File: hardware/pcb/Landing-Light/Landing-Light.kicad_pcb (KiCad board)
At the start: 2 copper layers, 70 x 20 mm, 56 parts, among them J1 Conn_01x04, J2 2012670005, Q2 NMOS, Q3 NMOS, Q4 PMOS, SW2 SW_SP3T, SW3 SW_SPDT, U1 BQ25172DSGR, U3 TPS61200DRC

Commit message: v1 Production
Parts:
- moved Q4 0.09 mm to (154.6, 94.2), turned to 90 degrees
- turned JP5 to -90 degrees
- turned R20 to 90 degrees
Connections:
- Q3 pad 1: GND -> -BATT
- Q3 pad 3: -BATT -> GND
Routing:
- net GND: track 43.9 -> 51.7 mm, vias 33 -> 34
- net +5V: track 53.2 -> 51.0 mm
- net Net-(JP6-A): track 7.22 -> 5.26 mm
- net -BATT: track 12.1 -> 11.4 mm
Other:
- board text added: "Landing Light v1.0"
- board text added: "STAT"
- board text added: "TT"

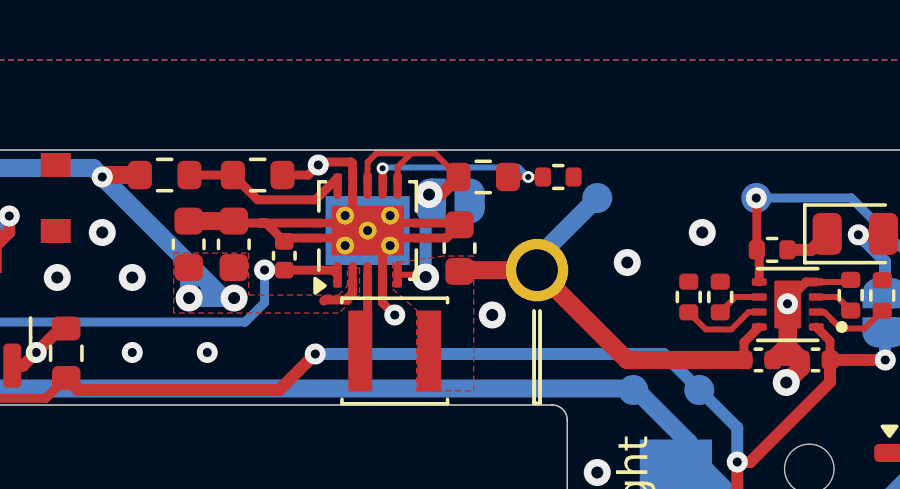
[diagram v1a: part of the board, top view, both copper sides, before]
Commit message: Fix via sizes
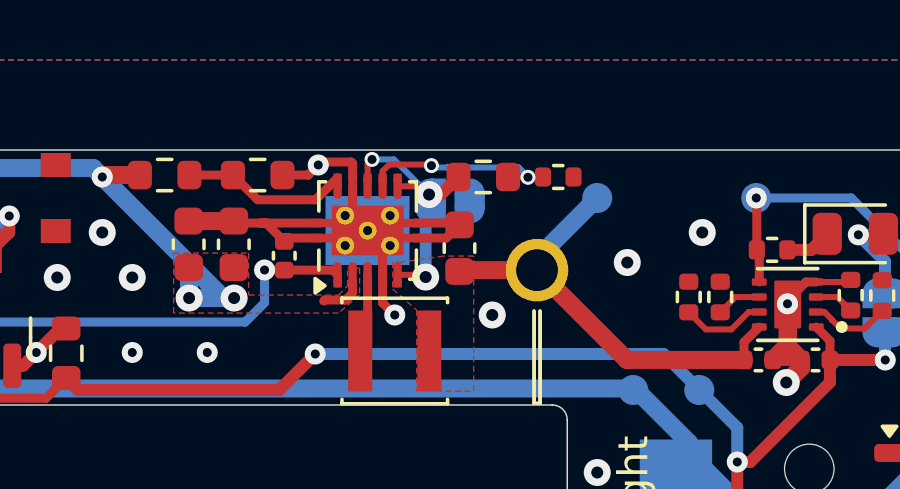
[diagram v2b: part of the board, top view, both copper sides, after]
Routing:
- net +BATT: track 25.3 -> 24.5 mm, vias 2 -> 3
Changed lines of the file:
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@@
-	)
-	(segment
-		(start 168.345 88.566726)
-		(end 168.8 88.111726)
-		(width 0.2)
-		(layer "F.Cu")
-		(net 1)
 	)
 	(segment
@@
 	)
 	(segment
-		(start 169.586726 88.111726)
-		(end 170.375 88.9)
-		(width 0.2)
-		(layer "F.Cu")
-		(net 1)
-	)
-	(segment
-		(start 167.637893 88.111726)
-		(end 168.8 88.111726)
-		(width 0.2)
-		(layer "F.Cu")
-		(net 1)
-	)
-	(segment
 		(start 169.789853 89.485147)
 		(end 170.375 88.9)
@@
 	)
 	(segment
+		(start 169.11794 89.21)
+		(end 169.393087 89.485147)
+		(width 0.2)
+		(layer "F.Cu")
+		(net 1)
+	)
+	(segment
 		(start 179.868 95.022)
 		(end 179.892 94.998)
@@
 	)
 	(segment
-		(start 167.345 88.404619)
-		(end 167.637893 88.111726)
-		(width 0.2)
-		(layer "F.Cu")
-		(net 1)
-	)
-	(segment
 		(start 172.9925 92.005)
 		(end 175.9855 94.998)
@@
 	)
 	(segment
-		(start 168.8 88.111726)
-		(end 169.586726 88.111726)
+		(start 168.345 89.21)
+		(end 169.11794 89.21)
 		(width 0.2)
 		(layer "F.Cu")
@@
 	)
 	(segment
-		(start 168.345 88.925)
-		(end 168.345 88.566726)
+		(start 167.345 88.462537)
+		(end 167.492655 88.314882)
 		(width 0.2)
 		(layer "F.Cu")
@@
 	)
 	(segment
-		(start 167.345 88.925)
-		(end 167.345 88.404619)
-		(width 0.2)
-		(layer "F.Cu")
-		(net 1)
-	)
-	(segment
 		(start 169.205 92.16)
 		(end 169.28 92.235)
@@
 	)
 	(segment
+		(start 167.345 88.925)
+		(end 167.345 88.462537)
+		(width 0.2)
+		(layer "F.Cu")
+		(net 1)
+	)
+	(segment
 		(start 168.345 92.16)
 		(end 169.205 92.16)
@@
 		(net 1)
 	)
+	(via
+		(at 167.492655 88.314882)
+		(size 0.5)
+		(drill 0.3)
+		(layers "F.Cu" "B.Cu")
+		(net 1)
+	)
 	(segment
 		(start 169.28 89.598234)
@@
 	)
 	(segment
+		(start 167.492655 88.314882)
+		(end 168.222822 88.314882)
+		(width 0.2)
+		(layer "B.Cu")
+		(net 1)
+	)
+	(segment
+		(start 168.222822 88.314882)
+		(end 169.393087 89.485147)
+		(width 0.2)
+		(layer "B.Cu")
+		(net 1)
+	)
+	(segment
 		(start 172.9925 91.6075)
 		(end 175 89.6)
@@
 	)
 	(segment
+		(start 169.436927 88.485)
+		(end 168.065 88.485)
+		(width 0.2)
+		(layer "F.Cu")
+		(net 47)
+	)
+	(segment
+		(start 169.471927 88.52)
+		(end 169.436927 88.485)
+		(width 0.2)
+		(layer "F.Cu")
+		(net 47)
+	)
+	(segment
+		(start 168.065 88.485)
+		(end 167.845 88.705)
+		(width 0.2)
+		(layer "F.Cu")
+		(net 47)
+	)
+	(segment
 		(start 172.7 88.9)
+		(end 172.69 88.91)
+		(width 0.2)
+		(layer "F.Cu")
+		(net 47)
+	)
+	(segment
+		(start 172.69 88.91)
 		(end 172.025 88.9)
+		(width 0.2)
+		(layer "F.Cu")
+		(net 47)
+	)
+	(segment
+		(start 167.845 88.705)
+		(end 167.845 88.925)
 		(width 0.2)
 		(layer "F.Cu")
@@
 		(net 47)
 	)
-	(segment
-		(start 167.845 88.611726)
-		(end 167.845 89.21)
-		(width 0.2)
-		(layer "F.Cu")
+	(via
+		(at 169.471927 88.52)
+		(size 0.5)
+		(drill 0.3)
+		(layers "F.Cu" "B.Cu")
 		(net 47)
 	)
 	(via
-		(at 172.7 88.9)
-		(size 0.4)
-		(drill 0.2)
-		(layers "F.Cu" "B.Cu")
-		(net 47)
-	)
-	(via
-		(at 167.845 88.611726)
-		(size 0.4)
-		(drill 0.2)
+		(at 172.69 88.91)
+		(size 0.5)
+		(drill 0.3)
 		(layers "F.Cu" "B.Cu")
 		(net 47)
@@
 	)
 	(segment
-		(start 167.845 88.611726)
-		(end 167.874295 88.582431)
+		(start 169.471927 88.52)
+		(end 169.534358 88.582431)
 		(width 0.2)
 		(layer "B.Cu")
@@
 	)
 	(segment
-		(start 167.874295 88.582431)
+		(start 169.534358 88.582431)
 		(end 170 88.582431)
 		(width 0.2)

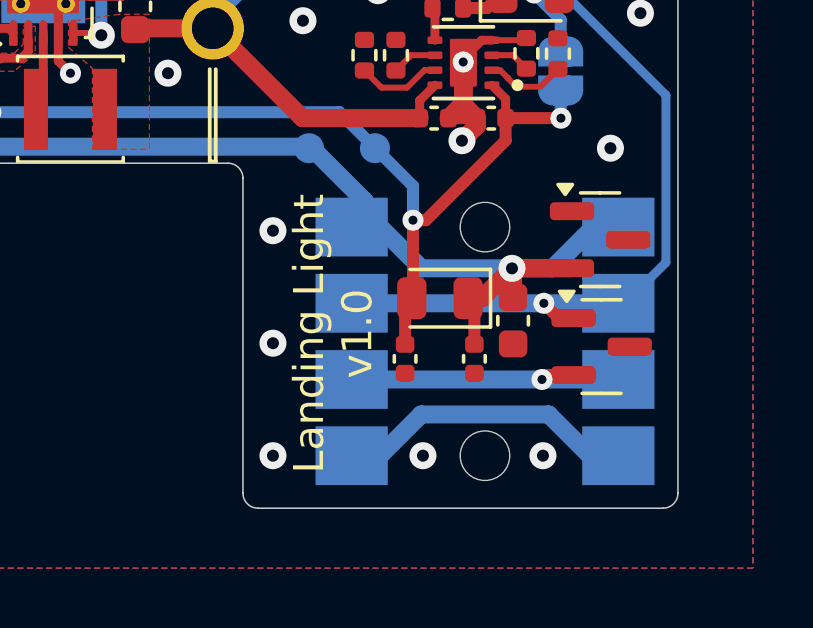
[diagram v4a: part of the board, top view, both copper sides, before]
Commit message: Update power routing
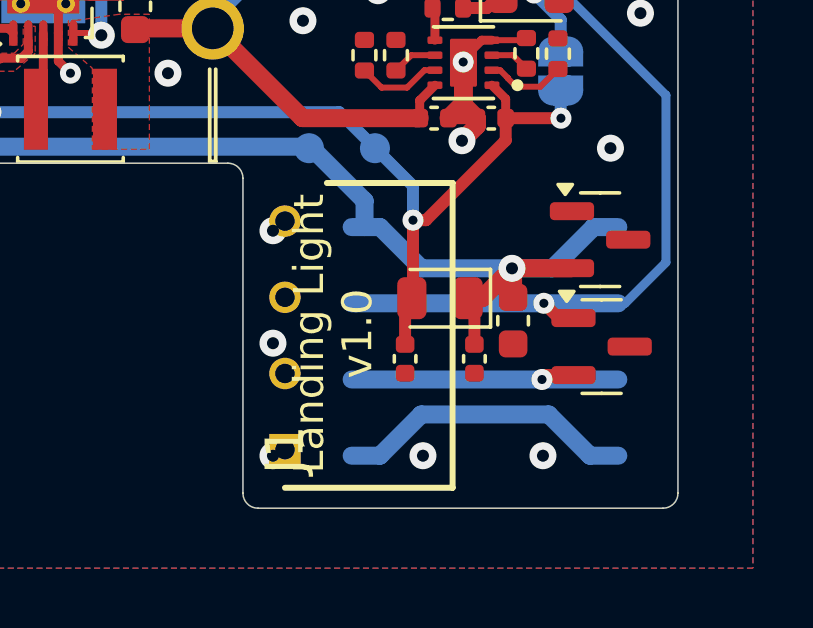
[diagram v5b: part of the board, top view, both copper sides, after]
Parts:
- J1: footprint Landing-Light:70AAJ-4-F1G -> MHCI:399-10-104-10-008000; moved to F.Cu
- moved J1 7.58 mm to (175.4, 106.0), turned to -90 degrees
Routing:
- net DATA2: track 10.0 -> 20.0 mm
- net GND: track 51.7 -> 41.7 mm

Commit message: Complete redesign - starting point
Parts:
- removed D2, D3, D4: D_TVS_Dual_AAC, Package_TO_SOT_SMD:SOT-23
- removed J2: 2012670005, Landing-Light:MOLEX_2012670005
- removed JP3, JP5, JP6: Jumper_2_Open, Jumper:SolderJumper-2_P1.3mm_Open_RoundedPad1.0x1.5mm
- removed R1, R9: 75R, Resistor_SMD:R_0402_1005Metric
- removed SW3: SW_SPDT, Landing-Light:SSSS810201
- added J3: USB_C_Receptacle_USB2.0_16P, Connector_USB:USB_C_Receptacle_G-Switch_GT-USB-7010ASV, F.Cu at (120.8, 101.6)
- added SW1: SW_SPDT, Landing-Light:SSSS810201, F.Cu at (149.0, 89.6)
- added U2: SRV05-4, Package_TO_SOT_SMD:SOT-363_SC-70-6, F.Cu at (177.1, 105.8)
- R8: value 75R -> TC33X-2-501E; footprint Resistor_SMD:R_0402_1005Metric -> Potentiometer_SMD:Potentiometer_Bourns_TC33X_Vertical
- moved TP7 27.3 mm to (203.5, 94.4)
- moved TP2 27.3 mm to (205.7, 94.4)
- moved TP1 25.5 mm to (181.4, 64.9)
- moved L2 24.8 mm to (159.2, 71.6), turned to 0 degrees
- moved R4 22.6 mm to (155.4, 75.7), turned to 90 degrees
- moved TP6 21.4 mm to (168.0, 73.8), turned to 180 degrees
- moved C12 21.1 mm to (157.0, 75.0), turned to -90 degrees
- moved R2 19.1 mm to (191.8, 75.6)
- moved R6 19.1 mm to (192.8, 75.6)
- moved D6 19.1 mm to (191.9, 73.6)
- moved R16 19.1 mm to (189.1, 74.1)
- moved R7 19.1 mm to (187.4, 75.7)
- moved U1 19.1 mm to (189.6, 75.9)
- moved C1 19.1 mm to (190.5, 77.8)
- moved C2 19.1 mm to (188.6, 77.8)
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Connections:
- net Net-(D7-RA) renamed /R
- net Net-(JP4-B) renamed /UVLO
- net Net-(U1-ISET) renamed /ISET
- net Net-(U1-TMR) renamed /TMR
- net Net-(U1-TS) renamed /TS
- net Net-(U1-VSET) renamed /VSET
- net Net-(U3-FB) renamed /FB
- net Net-(U3-L) renamed /L
- C12 pad 1: +BATT -> /VCC_SW
- D7 pad 2: Net-(D7-K) -> /Anode
- D7 pad 3: Net-(D7-GA) -> /G
- D7 pad 4: Net-(D7-BA) -> /B
- JP4 pad 1: +BATT -> /VCC_SW
- L2 pad 1: +BATT -> /VCC_SW
- Q2 pad 1: Net-(JP3-A) -> /Anode_R
- Q4 pad 3: Net-(JP6-A) -> /Anode_R
- R12 pad 1: GND -> /CC1
- R12 pad 2: /CC1 -> GND
- R13 pad 1: Net-(R1-Pad2) -> /R_R
- R3 pad 1: +BATT -> /VCC_SW
- R8 pad 1: Net-(R8-Pad1) -> /Anode
- R8 pad 2: Net-(D7-GA) -> /Anode_R
- SW2 pad 1: Net-(R9-Pad1) -> /B
- SW2 pad 2: Net-(R8-Pad1) -> /G
- SW2 pad 4: Net-(R1-Pad1) -> /R_R
- U3 pad 5: +BATT -> /VCC_SW
- U3 pad 6: +BATT -> /VCC_SW
- U3 pad 8: +BATT -> /VCC_SW
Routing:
- net VIN: track 81.4 -> 0.00 mm, vias 2 -> 0
- net +5V: track 51.0 -> 3.34 mm, vias 3 -> 1
- net VAUX: track 39.9 -> 1.84 mm, vias 2 -> 0
- net +3V3: track 34.5 -> 0.00 mm, vias 4 -> 0
- net Net-(D7-K): track 31.8 -> 0.00 mm, vias 2 -> 0
- net CHARGE_STATUS: track 30.4 -> 1.11 mm, vias 2 -> 0
- net /CC1: track 28.5 -> 0.00 mm, vias 2 -> 0
- net /CC2: track 27.4 -> 0.00 mm, vias 2 -> 0
- net +BATT: track 24.5 -> 1.31 mm, vias 3 -> 0
- net GND: track 41.7 -> 21.5 mm, vias 34 -> 0
- net DATA2: track 20.0 -> 0.00 mm, vias 1 -> 0
- net Net-(R9-Pad1): track 15.3 -> 0.00 mm
- net Net-(R8-Pad1): track 10.3 -> 0.00 mm
- net Net-(D7-GA): track 8.84 -> 0.00 mm
- net -BATT: track 11.4 -> 2.94 mm
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- added copper zone on F.Cu, net /L
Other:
- board size 70 x 20 mm -> 61.5 x 20 mm
- board text removed: "BATT-"
- board text removed: "REV"

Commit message: Routing complete
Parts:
- removed JP2: Jumper_2_Open, Jumper:SolderJumper-2_P1.3mm_Open_RoundedPad1.0x1.5mm
- added H1: MountingHole, MountingHole:MountingHole_2.2mm_M2, F.Cu at (178.8, 105.6)
- added H2: MountingHole, MountingHole:MountingHole_2.2mm_M2, F.Cu at (178.8, 89.4)
- added R9: 27k, Resistor_SMD:R_0402_1005Metric, F.Cu at (147.7, 89.4)
- R10: footprint Resistor_SMD:R_0603_1608Metric -> Resistor_SMD:R_0402_1005Metric
- R11: value 180k -> 150k; footprint Resistor_SMD:R_0603_1608Metric -> Resistor_SMD:R_0402_1005Metric
- R3: value 180k -> 510k; footprint Resistor_SMD:R_0603_1608Metric -> Resistor_SMD:R_0402_1005Metric
- R4: value 470k -> 200k
- moved TP2 29.6 mm to (176.2, 92.1), turned to 90 degrees
- moved TP5 28.8 mm to (166.3, 90.7)
- moved D6 28.7 mm to (169.6, 91.7)
- moved R6 28.7 mm to (170.5, 93.7)
- moved R7 28.7 mm to (165.1, 93.8)
- moved U1 28.7 mm to (167.3, 94.0)
- moved C1 28.7 mm to (168.2, 95.9)
- moved R2 28.7 mm to (169.5, 93.7)
- moved C2 28.7 mm to (166.3, 95.9)
- moved R5 28.7 mm to (164.0, 93.8)
- moved R16 28.4 mm to (166.8, 91.7)
- moved TP6 28.2 mm to (146.0, 91.5), turned to 0 degrees
- moved C3 26.6 mm to (144.5, 90.8), turned to 90 degrees
- moved TP1 25.6 mm to (173.2, 89.2)
- moved R10 25.2 mm to (144.3, 88.8), turned to 0 degrees
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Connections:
- D6 pad 2: Net-(D6-A) -> +5V
- R11 pad 2: GND -> Net-(R11-Pad2)
- SW1 pad 1: /VCC_SW -> +BATT
- SW1 pad 2: +BATT -> /VCC_SW
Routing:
- net VIN: track 0.00 -> 110.6 mm, vias 0 -> 2
- net /CC2: track 0.00 -> 67.0 mm, vias 0 -> 2
- net /CC1: track 0.00 -> 59.3 mm, vias 0 -> 2
- net +5V: track 3.34 -> 51.7 mm, vias 1 -> 6
- net VAUX: track 1.84 -> 28.7 mm, vias 0 -> 2
- net /VCC_SW: track 1.74 -> 28.0 mm, vias 1 -> 3
- net CHARGE_STATUS: track 1.11 -> 26.8 mm, vias 0 -> 1
- net +BATT: track 1.31 -> 26.3 mm
- net +3V3: track 0.00 -> 24.1 mm
- net /G: track 0.00 -> 23.3 mm
- net /B: track 0.00 -> 22.9 mm
- net GND: track 21.5 -> 42.2 mm, vias 0 -> 25
- net /Anode: track 0.00 -> 11.5 mm
- net /Anode_R: track 0.00 -> 10.7 mm
- net /R_R: track 0.00 -> 6.74 mm
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- added copper zone on F.Cu, net /VCC_SW
- removed copper zone on F.Cu, net +3V3
- removed copper zone on F.Cu, net +BATT
- removed copper zone on F.Cu, net /L
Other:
- board size 61.5 x 20 mm -> 62.8 x 21 mm
- board text added: "Landing Light v1.1"
- board text removed: "Landing Light v1.0"
- board text removed: "NMOS"
- board text removed: "PMOS"

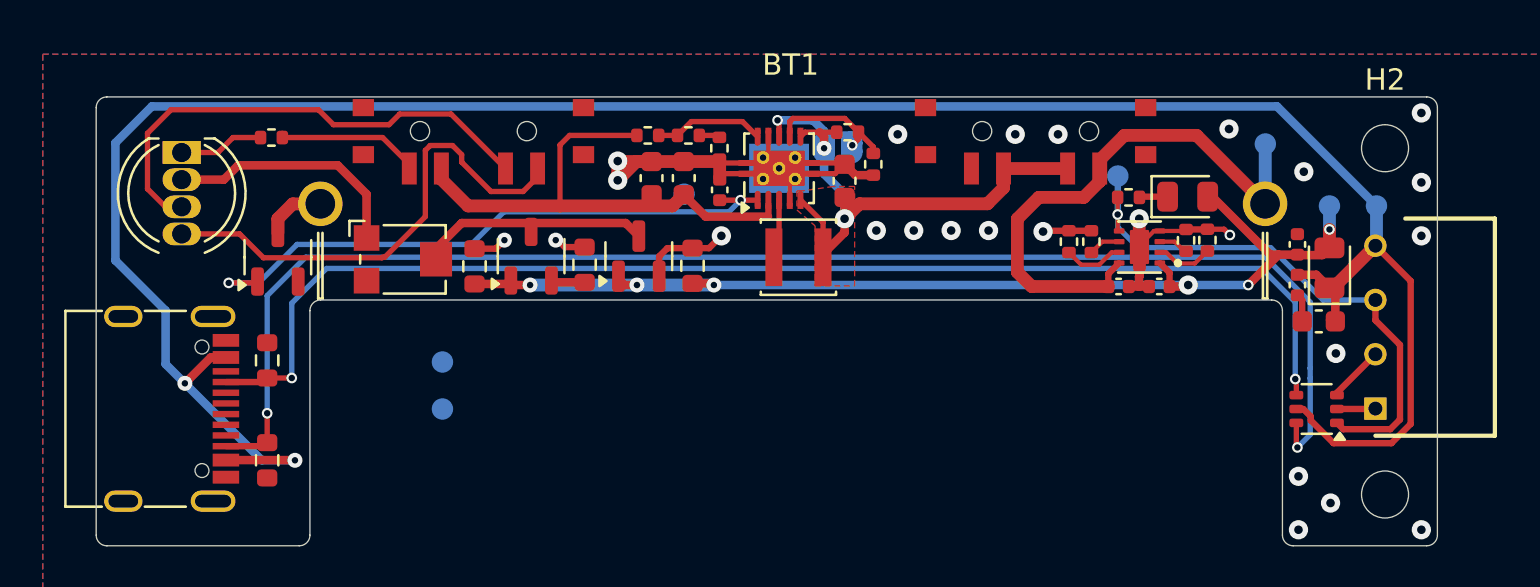
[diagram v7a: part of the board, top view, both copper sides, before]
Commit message: Tidying via placement
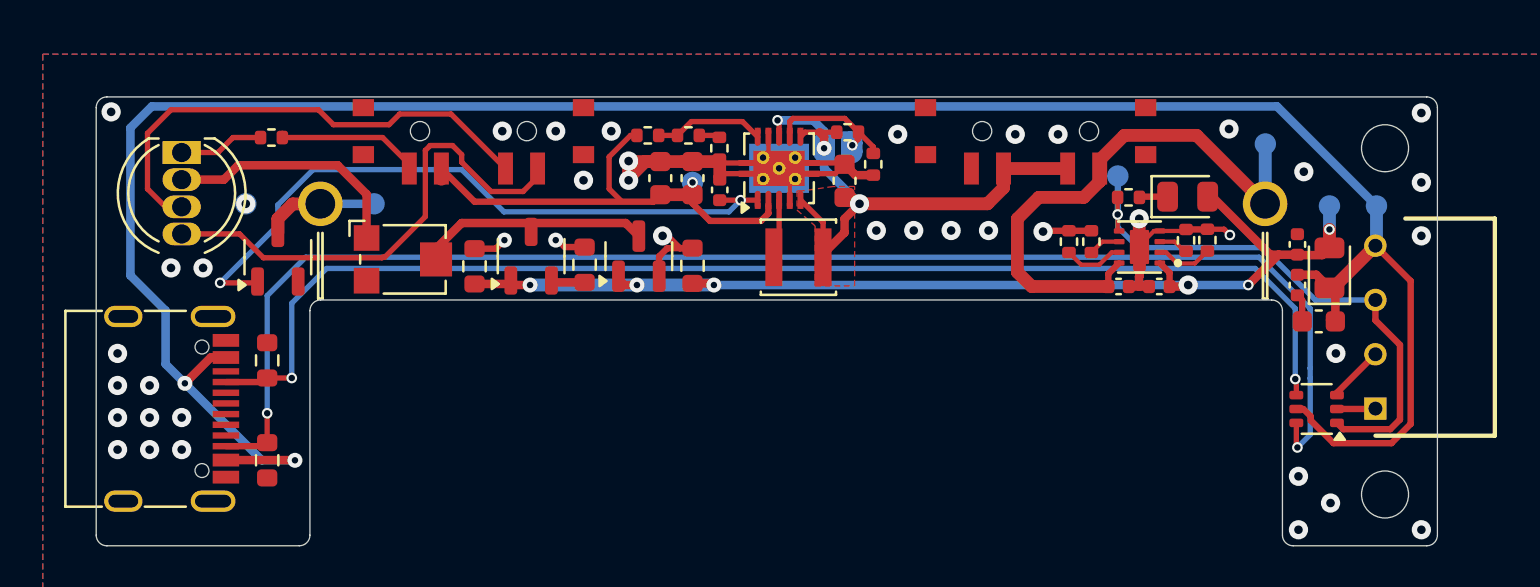
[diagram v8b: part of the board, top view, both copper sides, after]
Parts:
- moved TP3 13.3 mm to (125.5, 92.0)
- moved TP4 8.06 mm to (131.5, 92.0)
- moved TP6 0.68 mm to (146.4, 91.0)
- moved C11 0.41 mm to (146.4, 90.8)
- moved C3 0.41 mm to (144.9, 90.8)
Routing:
- net VAUX: track 28.7 -> 31.7 mm
- net -BATT: track 2.94 -> 5.46 mm
- net +3V3: track 24.1 -> 22.5 mm, vias 0 -> 1
- net /VCC_SW: track 28.0 -> 27.4 mm
- net VIN: track 110.6 -> 110.0 mm
- net GND: track 42.2 -> 42.0 mm, vias 25 -> 42
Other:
- board text added: "-BATT"
- board text removed: "CHRG LED"
